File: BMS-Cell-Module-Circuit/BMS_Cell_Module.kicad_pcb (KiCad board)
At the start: 2 copper layers, 54 x 80 mm, 46 parts, among them J1 Conn_01x04_Female, J2 Conn_01x04_Female, J3 Conn_01x02_Male, M1 SI2312BDS-T1-E3, U1 MCP1703A-3302_SOT223, U2 ADUM1250ARZ, U3 ATTINY85-20SU

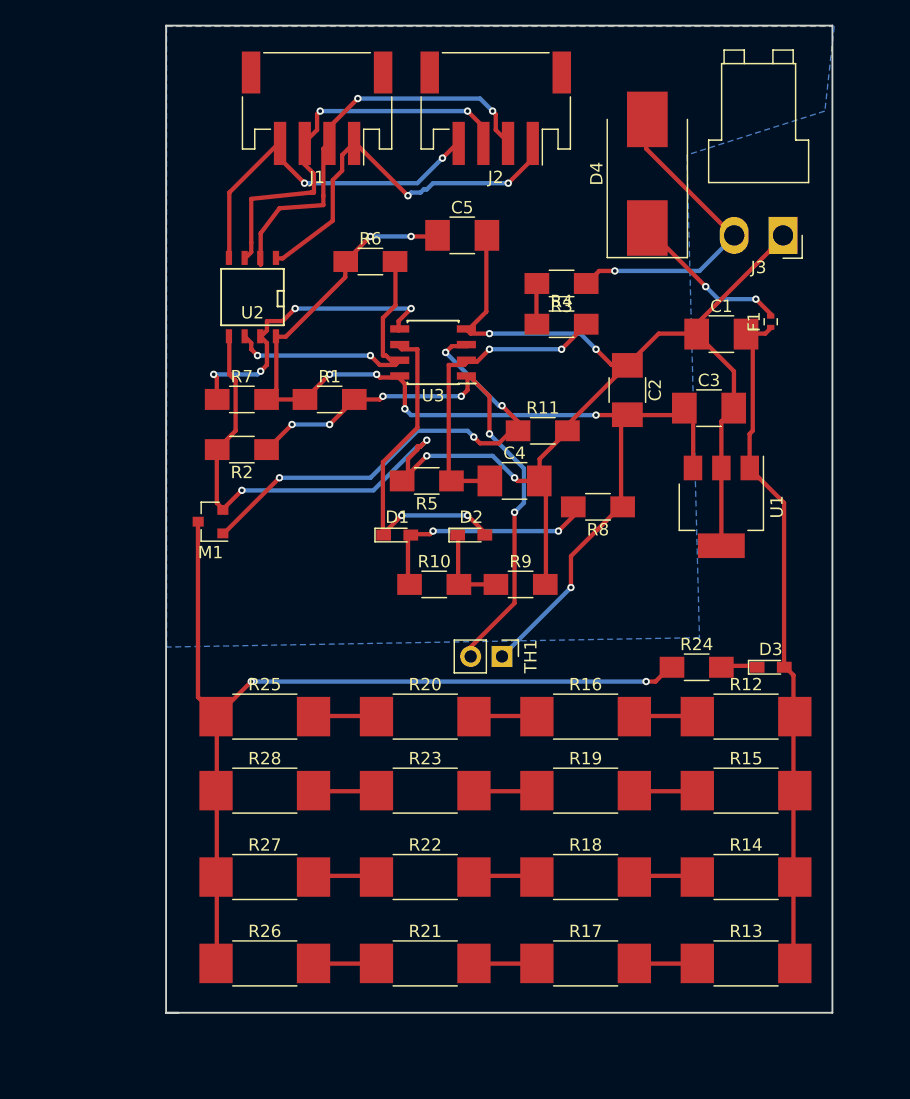
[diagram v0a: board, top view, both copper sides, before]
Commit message: Started work on PCB
DONT USE THIS PCB FOR PRODUCTION!
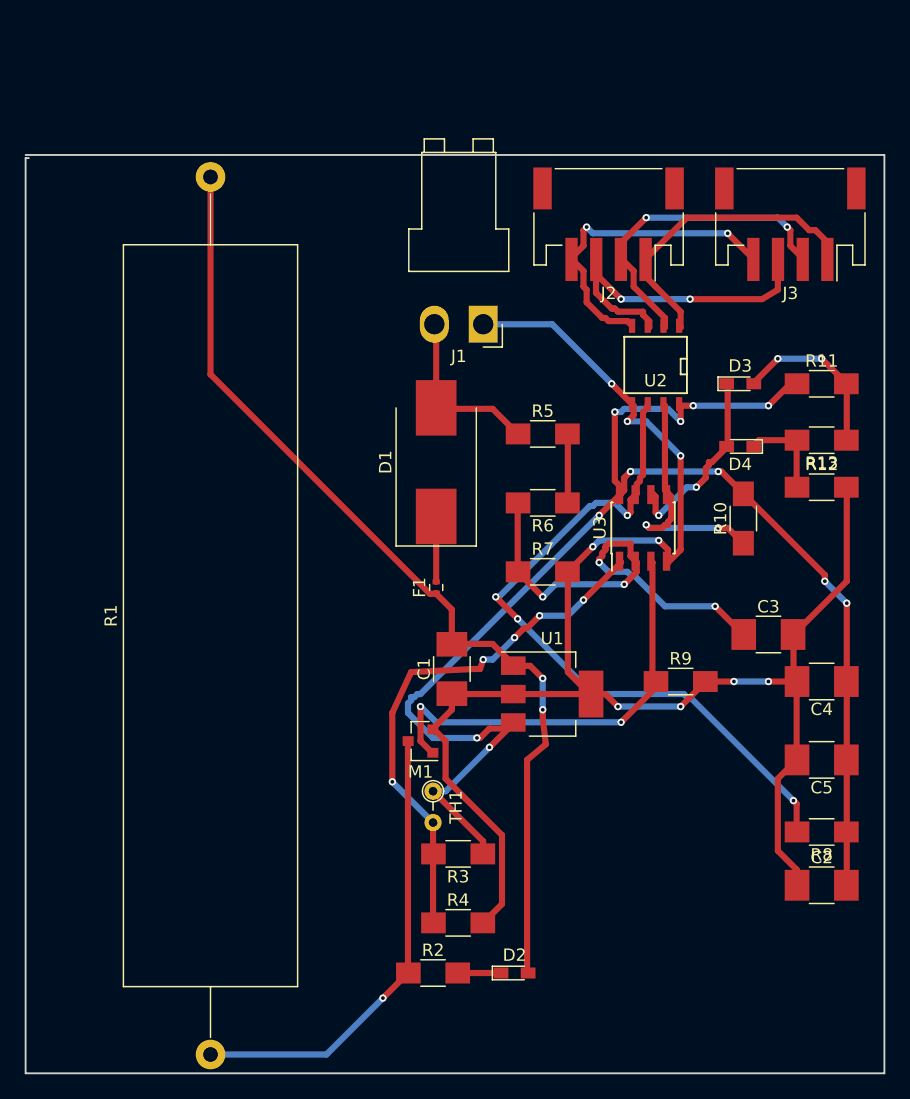
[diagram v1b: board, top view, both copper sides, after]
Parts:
- removed R14, R15, R16, R17, R18, R19, R20, R21, R22, R23, R25, R26, R27: 3R3 1W, Resistors_SMD:R_2512_HandSoldering
- removed R24: 47R 1/4W, Resistors_SMD:R_1206_HandSoldering
- removed R28: RC2512JK-073R3L 3R3 2512 [6432 Metric], Resistors_SMD:R_2512_HandSoldering
- D1: value LED RED -> S3D-E3/57T 3A; footprint LEDs:LED_0603_HandSoldering -> Diodes_SMD:D_SMC_Handsoldering
- D2: value LED GREEN -> LED BLUE KPL-3015QBC-D
- D3: value LED BLUE KPL-3015QBC-D -> LED RED
- D4: value S3D-E3/57T 3A -> LED GREEN; footprint Diodes_SMD:D_SMC_Handsoldering -> LEDs:LED_0603_HandSoldering
- F1: value Fuse, 2A, 32VDC, Fast Acting ERBRD2R00X -> Fuse
- J1: value Conn_01x04_Female -> Conn_01x02_Male; footprint Connectors_JST:JST_PH_S4B-PH-SM4-TB_04x2.00mm_Angled -> Connectors_JST:JST_VH_B2PS-VH_2x2x3.96mm_Horizontal
- J2: value Conn_01x04_Female -> DATA
- J3: value Conn_01x02_Male -> DATA; footprint Connectors_JST:JST_VH_B2PS-VH_2x2x3.96mm_Horizontal -> Connectors_JST:JST_PH_S4B-PH-SM4-TB_04x2.00mm_Angled
- M1: value SI2312BDS-T1-E3 -> SI2312BDS
- R1: value 20K -> HS50 3R3 J 50W Axial Wire Wound; footprint Resistors_SMD:R_1206_HandSoldering -> Resistors_THT:R_Axial_Power_L60.0mm_W14.0mm_P71.12mm
- R11: value 47K -> 510R
- R12: value 3R3 1W -> 510R; footprint Resistors_SMD:R_2512_HandSoldering -> Resistors_SMD:R_1206_HandSoldering
- R13: value 3R3 1W -> 2K2; footprint Resistors_SMD:R_2512_HandSoldering -> Resistors_SMD:R_1206_HandSoldering
- R2: value 10K -> 47R 1/4W
- R3: value 47K -> 20K
- R4: value 470K -> 10K
- R5: value 680K -> 47K
- R6: value 2K2 -> 470K
- R7: value 2K2 -> 680K
- R8: value 510R -> 2K2
- R9: value 510R -> 47K
- TH1: footprint Pin_Headers:Pin_Header_Straight_1x02_Pitch2.54mm -> Resistors_THT:R_Axial_DIN0204_L3.6mm_D1.6mm_P2.54mm_Vertical
- U1: value MCP1703A-3302_SOT223 -> MCP1703A
- moved R1 54.0 mm to (117.6, 135.4), turned to 90 degrees
- moved C5 51.5 mm to (167.1, 111.5), turned to 180 degrees
- moved R4 49.2 mm to (137.7, 124.7)
- moved R3 47.0 mm to (137.7, 119.1)
- moved R2 45.2 mm to (135.6, 128.8), turned to 0 degrees
- moved C2 43.1 mm to (167.1, 121.7), turned to 0 degrees
- moved R13 42.8 mm to (167.1, 85.6), turned to 180 degrees
- moved D2 35.7 mm to (142.2, 128.8)
- moved C1 34.8 mm to (137.2, 104.1), turned to 90 degrees
- moved F1 34.6 mm to (135.9, 97.5)
- moved U2 33.1 mm to (153.7, 79.5)
- moved R8 32.0 mm to (167.1, 117.3)
- moved C4 29.7 mm to (167.1, 105.2), turned to 180 degrees
- moved R7 28.1 mm to (144.5, 96.3)
- moved R10 25.6 mm to (160.8, 91.9), turned to 90 degrees
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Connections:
- C3 pad 1: 3V3 -> Net-(C3-Pad1)
- C4 pad 1: Net-(C4-Pad1) -> 3V3
- D1 pad 2: Net-(D1-Pad2) -> BATT+RAW
- D2 pad 2: Net-(D1-Pad1) -> BATT+
- D3 pad 2: BATT+ -> Net-(D3-Pad2)
- D4 pad 2: BATT+RAW -> Net-(D3-Pad1)
- F1 pad 2: Net-(D4-Pad1) -> Net-(D1-Pad1)
- J1 pad 1: Net-(J1-Pad1) -> GND
- J1 pad 2: Net-(J1-Pad2) -> BATT+RAW
- J2 pad 1: Net-(J1-Pad1) -> Net-(J2-Pad1)
- J2 pad 2: Net-(J1-Pad2) -> Net-(J2-Pad2)
- J2 pad 3: Net-(J1-Pad3) -> Net-(J2-Pad3)
- J2 pad 4: Net-(J1-Pad4) -> Net-(J2-Pad4)
- J3 pad 1: GND -> Net-(J2-Pad1)
- J3 pad 2: BATT+RAW -> Net-(J2-Pad2)
- R1 pad 1: 3V3 -> Net-(M1-Pad3)
- R1 pad 2: Net-(R1-Pad2) -> BATT+
- R10 pad 1: Net-(D1-Pad2) -> Net-(R10-Pad1)
- R10 pad 2: Net-(D2-Pad1) -> 3V3
- R11 pad 1: Net-(M1-Pad1) -> 3V3
- R11 pad 2: GND -> Net-(D3-Pad2)
- R12 pad 1: Net-(R12-Pad1) -> Net-(D4-Pad1)
- R12 pad 2: BATT+ -> GND
- R13 pad 1: Net-(R13-Pad1) -> Net-(D3-Pad2)
- R13 pad 2: BATT+ -> Net-(D4-Pad1)
- R2 pad 1: Net-(R1-Pad2) -> Net-(M1-Pad3)
- R2 pad 2: GND -> Net-(D2-Pad1)
- R3 pad 1: BATT+RAW -> 3V3
- R4 pad 2: Net-(C4-Pad1) -> GND
- R5 pad 1: Net-(C4-Pad1) -> BATT+RAW
- R5 pad 2: GND -> Net-(R5-Pad2)
- R6 pad 1: 3V3 -> Net-(R5-Pad2)
- R6 pad 2: Net-(R6-Pad2) -> Net-(C3-Pad1)
- R7 pad 1: Net-(R7-Pad1) -> Net-(C3-Pad1)
- R7 pad 2: 3V3 -> GND
- R8 pad 2: Net-(D1-Pad2) -> Net-(R8-Pad2)
- R9 pad 1: Net-(D2-Pad1) -> Net-(M1-Pad1)
- TH1 pad 2: Net-(R1-Pad2) -> Net-(R3-Pad2)
- U2 pad 1: Net-(J1-Pad1) -> Net-(J2-Pad1)
- U2 pad 2: Net-(J1-Pad2) -> Net-(J2-Pad2)
- U2 pad 3: Net-(J1-Pad3) -> Net-(J2-Pad3)
- U2 pad 4: Net-(J1-Pad4) -> Net-(J2-Pad4)
- U2 pad 6: Net-(R6-Pad2) -> Net-(R8-Pad2)
- U2 pad 7: Net-(R7-Pad1) -> Net-(R10-Pad1)
- U3 pad 1: Net-(R1-Pad2) -> Net-(R3-Pad2)
- U3 pad 2: Net-(C4-Pad1) -> Net-(C3-Pad1)
- U3 pad 5: Net-(R7-Pad1) -> Net-(R10-Pad1)
- U3 pad 6: Net-(D1-Pad1) -> Net-(D3-Pad1)
- U3 pad 7: Net-(R6-Pad2) -> Net-(R8-Pad2)
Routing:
- net Net-(R8-Pad2): track 0.00 -> 57.9 mm, vias 0 -> 4
- net Net-(R1-Pad2): track 46.1 -> 0.00 mm, vias 6 -> 0
- net Net-(R3-Pad2): track 3.37 -> 43.1 mm, vias 0 -> 5
- net Net-(M1-Pad3): track 75.8 -> 37.6 mm, vias 2 -> 1
- net Net-(C3-Pad1): track 0.00 -> 37.6 mm, vias 0 -> 4
- net Net-(J1-Pad2): track 33.7 -> 0.00 mm, vias 2 -> 0
- net 3V3: track 90.1 -> 123.6 mm, vias 7 -> 11
- net Net-(J1-Pad3): track 32.9 -> 0.00 mm, vias 2 -> 0
- net Net-(J1-Pad1): track 31.8 -> 0.00 mm, vias 2 -> 0
- net Net-(J1-Pad4): track 29.4 -> 0.00 mm, vias 2 -> 0
- net Net-(J2-Pad3): track 0.00 -> 28.7 mm, vias 0 -> 2
- net Net-(J2-Pad1): track 0.00 -> 26.9 mm
- net Net-(J2-Pad2): track 0.00 -> 26.4 mm, vias 0 -> 2
- net Net-(J2-Pad4): track 0.00 -> 26.4 mm, vias 0 -> 2
- net Net-(C4-Pad1): track 25.5 -> 0.00 mm, vias 2 -> 0
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- removed copper zone on B.Cu, net GND
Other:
- board size 54 x 80 mm -> 69.6 x 74.4 mm

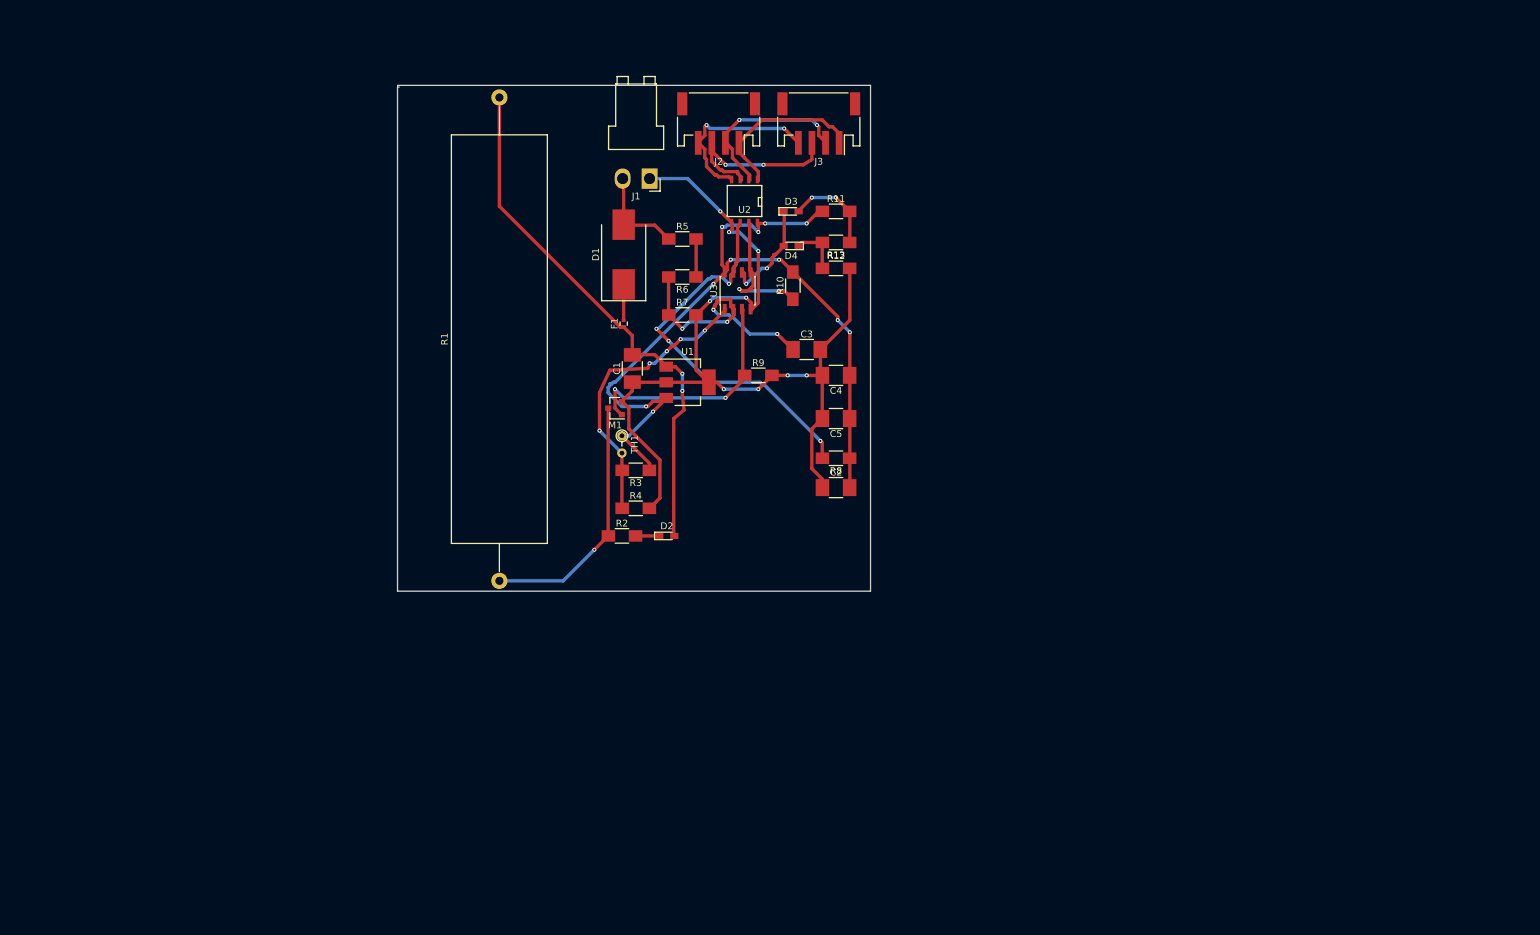
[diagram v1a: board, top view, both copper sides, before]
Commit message: Split board into two sections
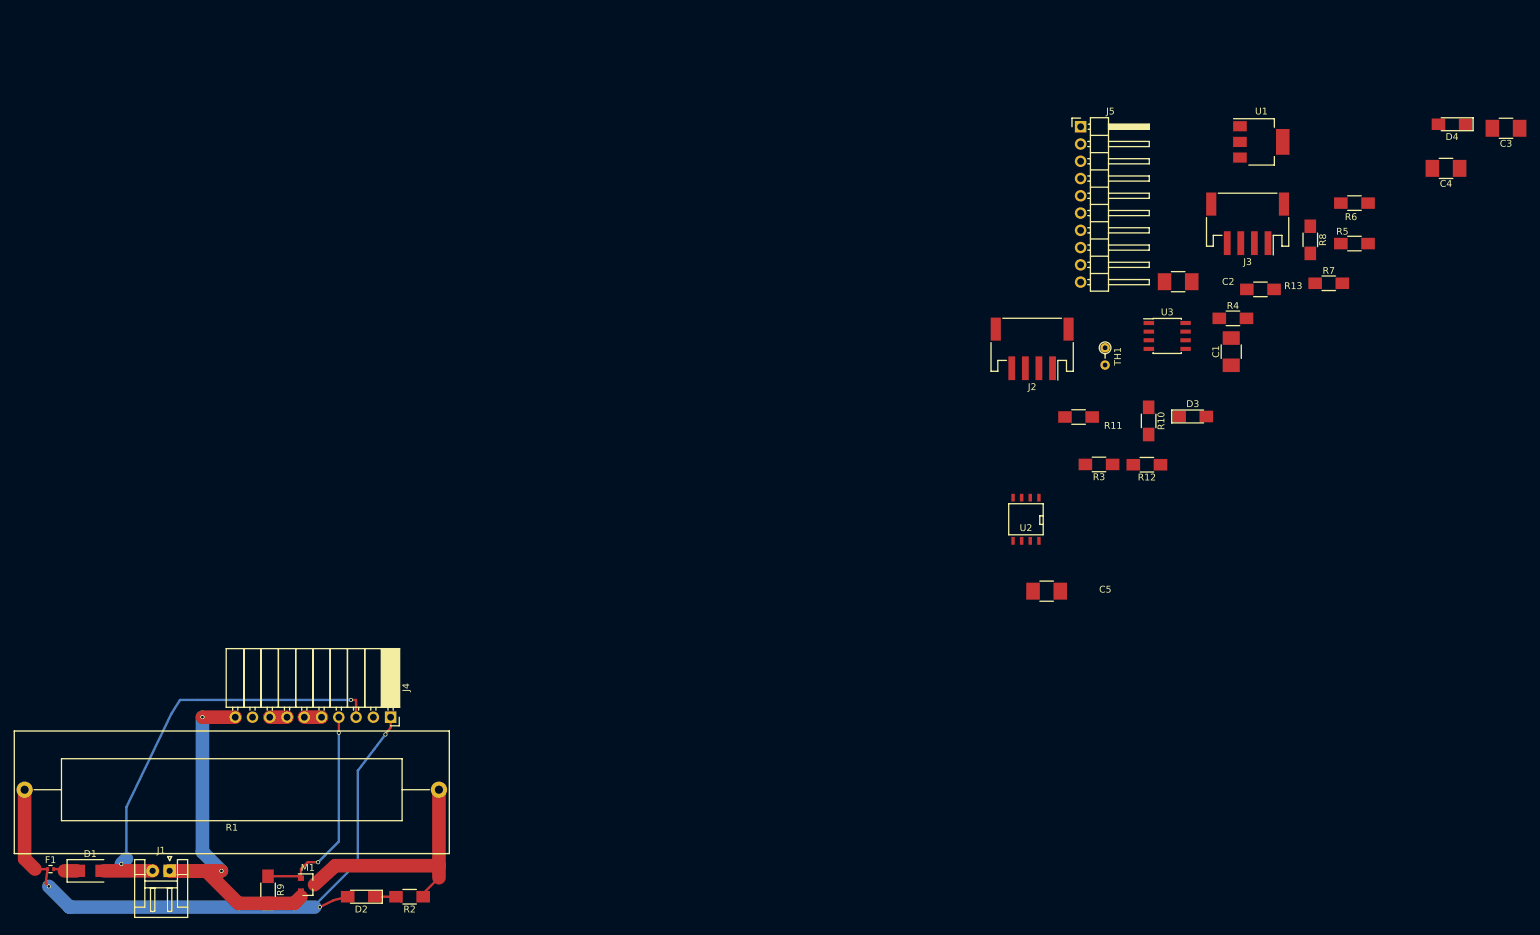
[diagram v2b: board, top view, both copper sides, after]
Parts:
- added J4: Conn Female, Socket_Strips:Socket_Strip_Angled_1x10_Pitch2.54mm, F.Cu at (101.6, 155.4)
- added J5: Conn Male, Pin_Headers:Pin_Header_Angled_1x10_Pitch2.54mm, F.Cu at (203.1, 68.6)
- D1: value S3D-E3/57T 3A -> SE30AFG-M3/6A; footprint Diodes_SMD:D_SMC_Handsoldering -> Diodes_SMD:D_SMA
- D2, D3, D4: footprint LEDs:LED_0603_HandSoldering -> LEDs:LED_1206_HandSoldering
- F1: value Fuse -> Fuse, 2A, 32VDC, Fast Acting ERBRD2R00X
- J1: footprint Connectors_JST:JST_VH_B2PS-VH_2x2x3.96mm_Horizontal -> Connectors_JST:JST_EH_S02B-EH_02x2.50mm_Angled
- J2, J3: value DATA -> Conn_01x04_Female
- M1: value SI2312BDS -> SI2312BDS-T1-E3
- R1: footprint Resistors_THT:R_Axial_Power_L60.0mm_W14.0mm_P71.12mm -> Resistors_THT:R_Axial_Power_L50.0mm_W9.0mm_P60.96mm
- U1: value MCP1703A -> MCP1703A-3302_SOT223
- moved J1 123.9 mm to (69.1, 178.1)
- moved D1 119.9 mm to (57.4, 178.1), turned to 0 degrees
- moved F1 116.4 mm to (51.6, 177.8), turned to 0 degrees
- moved C3 107.9 mm to (265.7, 68.8), turned to 180 degrees
- moved R9 104.6 mm to (83.6, 180.8), turned to 270 degrees
- moved R6 99.5 mm to (243.4, 79.8)
- moved R5 98.9 mm to (243.4, 85.8)
- moved D4 98.9 mm to (257.8, 68.2)
- moved R7 95.2 mm to (239.6, 91.6)
- moved C4 94.8 mm to (256.9, 74.7)
- moved R4 92.2 mm to (225.5, 96.8)
- moved U1 91.5 mm to (229.7, 70.8)
- moved C1 88.2 mm to (225.3, 101.7)
- moved M1 83.4 mm to (89.4, 180.1), turned to 0 degrees
- moved R8 76.8 mm to (236.9, 85.2), turned to 270 degrees
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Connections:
- C1 pad 1: GND -> GND2
- C1 pad 2: BATT+ -> Net-(C1-Pad2)
- C2 pad 1: GND -> GND2
- C3 pad 2: GND -> GND2
- C4 pad 2: GND -> GND2
- C5 pad 2: GND -> GND2
- M1 pad 1: Net-(M1-Pad1) -> Net-(J4-Pad4)
- R10 pad 1: Net-(R10-Pad1) -> Net-(J5-Pad6)
- R12 pad 2: GND -> GND2
- R4 pad 2: GND -> GND2
- R5 pad 1: BATT+RAW -> Net-(J5-Pad3)
- R7 pad 2: GND -> GND2
- R8 pad 2: Net-(R8-Pad2) -> Net-(J5-Pad8)
- R9 pad 1: Net-(M1-Pad1) -> Net-(J4-Pad4)
- U1 pad 1: BATT+ -> Net-(C1-Pad2)
- U1 pad 2: GND -> GND2
- U2 pad 5: GND -> GND2
- U2 pad 6: Net-(R8-Pad2) -> Net-(J5-Pad8)
- U2 pad 7: Net-(R10-Pad1) -> Net-(J5-Pad6)
- U3 pad 3: Net-(M1-Pad1) -> Net-(J5-Pad4)
- U3 pad 4: GND -> GND2
- U3 pad 5: Net-(R10-Pad1) -> Net-(J5-Pad5)
- U3 pad 7: Net-(R8-Pad2) -> Net-(J5-Pad7)
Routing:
- net 3V3: track 123.6 -> 0.00 mm, vias 11 -> 0
- net GND: track 139.9 -> 58.9 mm, vias 9 -> 2
- net Net-(R8-Pad2): track 57.9 -> 0.00 mm, vias 4 -> 0
- net BATT+RAW: track 14.5 -> 64.9 mm, vias 0 -> 2
- net Net-(J5-Pad9): track 43.1 -> 0.00 mm, vias 5 -> 0
- net Net-(C3-Pad1): track 37.6 -> 0.00 mm, vias 4 -> 0
- net Net-(M1-Pad1): track 35.5 -> 0.00 mm, vias 2 -> 0
- net Net-(J4-Pad4): track 0.00 -> 31.9 mm, vias 0 -> 2
- net Net-(J2-Pad3): track 28.7 -> 0.00 mm, vias 2 -> 0
- net Net-(J2-Pad1): track 26.9 -> 0.00 mm
- net Net-(J2-Pad2): track 26.4 -> 0.00 mm, vias 2 -> 0
- net Net-(J2-Pad4): track 26.4 -> 0.00 mm, vias 2 -> 0
- net Net-(R10-Pad1): track 21.0 -> 0.00 mm, vias 2 -> 0
- net Net-(D3-Pad1): track 16.0 -> 0.00 mm, vias 2 -> 0
- net BATT+: track 79.8 -> 94.6 mm, vias 2 -> 3
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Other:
- board outline removed
